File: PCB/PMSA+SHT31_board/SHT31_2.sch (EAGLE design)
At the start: 18 parts, among them CN2 CON_PINHD-2X15, Q3 MOSFET-NCHANNELBSS138, U2 SHT31-DIS, U3 MICS-4514

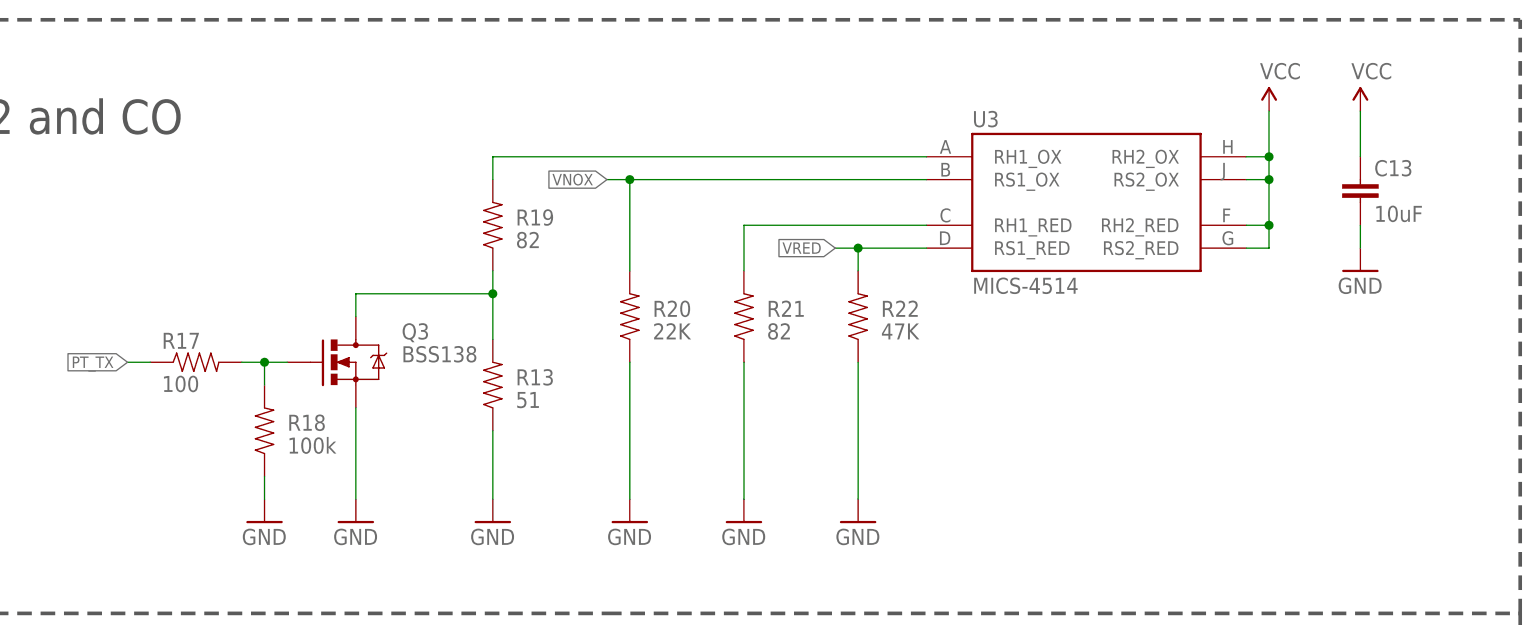
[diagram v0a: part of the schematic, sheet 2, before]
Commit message: insertion NOX & CO Captor
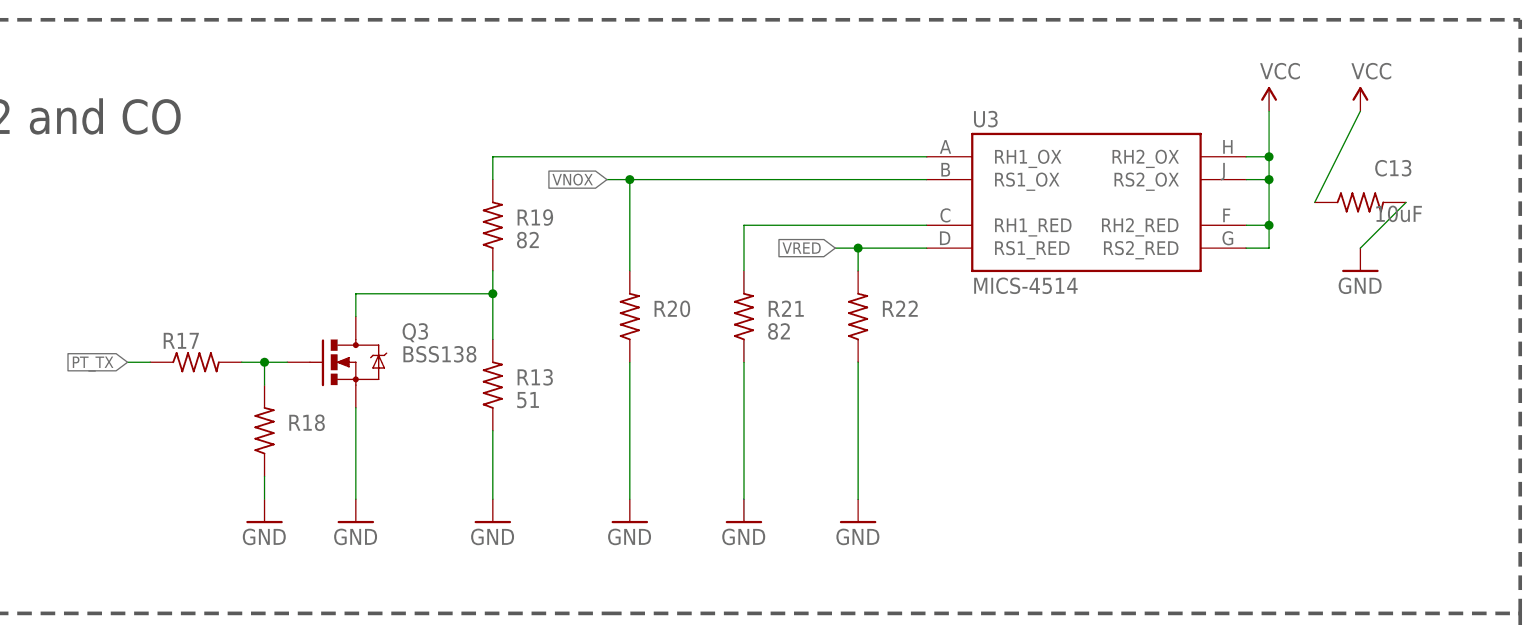
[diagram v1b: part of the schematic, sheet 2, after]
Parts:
- C13: device SparkFun-Capacitors:CAP0805 -> fab:RES-US1206FAB
- R13: device SparkFun-Resistors:RESISTOR0603 -> fab:RES-US1206FAB
- R17: device SparkFun-Resistors:100OHM1/10W1%(0603) -> fab:RES-US1206FAB
- R18: value 100k -> 100K; device SparkFun-Resistors:100KOHM1/10W1%(0603) -> fab:RES-US1206FAB
- R19, R21: device SparkFun-Resistors:RESISTOR0805-RES -> fab:RES-US1206FAB
- R20: device SparkFun-Resistors:22KOHM1/10W1%(0603) -> fab:RES-US1206FAB
- R22: device SparkFun-Resistors:47KOHM1/10W1%(0603) -> fab:RES-US1206FAB
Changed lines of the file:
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@@
 <part name="R9" library="microbuilder" deviceset="RESISTOR" device="_1206MP" value="10K"/>
 <part name="U$23" library="microbuilder" deviceset="VDD" device=""/>
-<part name="C13" library="SparkFun-Capacitors" deviceset="CAP" device="0805" value="10uF">
+<part name="C13" library="fab" deviceset="RES-US" device="1206FAB" value="10uF">
 <attribute name="PROD_ID" value="CAP-11330"/>
 </part>
@@
 <part name="GND24" library="SparkFun-Aesthetics" deviceset="GND" device=""/>
 <part name="U3" library="SparkFun-Sensors" deviceset="MICS-4514" device=""/>
-<part name="R13" library="SparkFun-Resistors" deviceset="RESISTOR" device="0603" value="51">
+<part name="R13" library="fab" deviceset="RES-US" device="1206FAB" value="51">
 <attribute name="PROD_ID" value="RES-12314"/>
 </part>
@@
 <attribute name="P_NAME" value="BSS138"/>
 </part>
-<part name="R17" library="SparkFun-Resistors" deviceset="100OHM1/10W1%(0603)" device="" value="100"/>
-<part name="R18" library="SparkFun-Resistors" deviceset="100KOHM1/10W1%(0603)" device="" value="100k"/>
+<part name="R17" library="fab" deviceset="RES-US" device="1206FAB" value="100"/>
+<part name="R18" library="fab" deviceset="RES-US" device="1206FAB" value="100K"/>
 <part name="GND25" library="SparkFun-Aesthetics" deviceset="GND" device=""/>
 <part name="GND26" library="SparkFun-Aesthetics" deviceset="GND" device=""/>
-<part name="R19" library="SparkFun-Resistors" deviceset="RESISTOR" device="0805-RES" value="82">
+<part name="R19" library="fab" deviceset="RES-US" device="1206FAB" value="82">
 <attribute name="DK_ID" value="541-82.0CCT-ND"/>
 </part>
-<part name="R20" library="SparkFun-Resistors" deviceset="22KOHM1/10W1%(0603)" device="" value="22K"/>
-<part name="R21" library="SparkFun-Resistors" deviceset="RESISTOR" device="0805-RES" value="82">
+<part name="R20" library="fab" deviceset="RES-US" device="1206FAB" value="22K"/>
+<part name="R21" library="fab" deviceset="RES-US" device="1206FAB" value="82">
 <attribute name="DK_ID" value="541-82.0CCT-ND"/>
 </part>
 <part name="GND27" library="SparkFun-Aesthetics" deviceset="GND" device=""/>
-<part name="R22" library="SparkFun-Resistors" deviceset="47KOHM1/10W1%(0603)" device="" value="47K"/>
+<part name="R22" library="fab" deviceset="RES-US" device="1206FAB" value="47K"/>
 <part name="GND28" library="SparkFun-Aesthetics" deviceset="GND" device=""/>
 <part name="P+3" library="SparkFun" deviceset="3.3V" device="" value="VCC"/>
@@
 <instance part="R17" gate="G$1" x="231.14" y="60.96" smashed="yes">
 <attribute name="NAME" x="227.33" y="62.4586" size="1.778" layer="95"/>
-<attribute name="VALUE" x="227.33" y="57.658" size="1.778" layer="96"/>
 </instance>
 <instance part="R18" gate="G$1" x="238.76" y="53.34" smashed="yes" rot="R90">
 <attribute name="NAME" x="241.3" y="53.34" size="1.778" layer="95"/>
-<attribute name="VALUE" x="241.3" y="50.8" size="1.778" layer="96"/>
 </instance>
 <instance part="GND25" gate="1" x="248.92" y="43.18" smashed="yes">
@@
 <instance part="R20" gate="G$1" x="279.4" y="66.04" smashed="yes" rot="R90">
 <attribute name="NAME" x="281.94" y="66.0146" size="1.778" layer="95"/>
-<attribute name="VALUE" x="281.94" y="63.5" size="1.778" layer="96"/>
 </instance>
 <instance part="R21" gate="G$1" x="292.1" y="66.04" smashed="yes" rot="R90">
@@
 <instance part="R22" gate="G$1" x="304.8" y="66.04" smashed="yes" rot="R90">
 <attribute name="NAME" x="307.34" y="66.0146" size="1.778" layer="95"/>
-<attribute name="VALUE" x="307.34" y="63.5" size="1.778" layer="96"/>
 </instance>
 <instance part="GND28" gate="1" x="304.8" y="43.18" smashed="yes">
@@
 <pinref part="C13" gate="G$1" pin="2"/>
 <pinref part="GND23" gate="1" pin="GND"/>
-<wire x1="360.68" y1="76.2" x2="360.68" y2="73.66" width="0.1524" layer="91"/>
+<wire x1="365.76" y1="78.74" x2="360.68" y2="73.66" width="0.1524" layer="91"/>
 </segment>
 <segment>
@@
 <pinref part="C13" gate="G$1" pin="1"/>
 <pinref part="P+4" gate="G$1" pin="3.3V"/>
-<wire x1="360.68" y1="83.82" x2="360.68" y2="88.9" width="0.1524" layer="91"/>
-</segment>
-</net>
+<wire x1="355.6" y1="78.74" x2="360.68" y2="88.9" width="0.1524" layer="91"/>
+</segment>
+</net>
